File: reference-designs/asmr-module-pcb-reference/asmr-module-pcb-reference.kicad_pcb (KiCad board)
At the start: 2 copper layers, 136 x 71 mm, 1 part

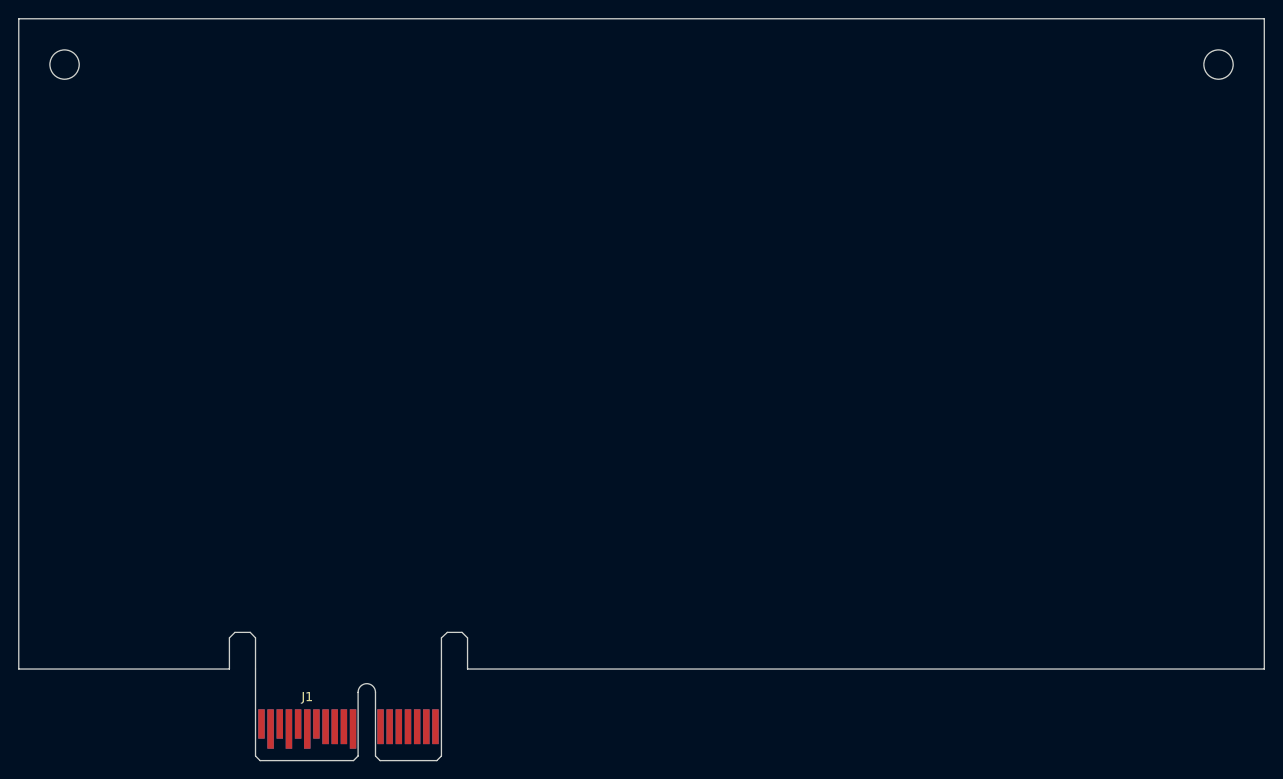
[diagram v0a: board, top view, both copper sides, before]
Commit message: Update reference design for 64-pin edge connector.
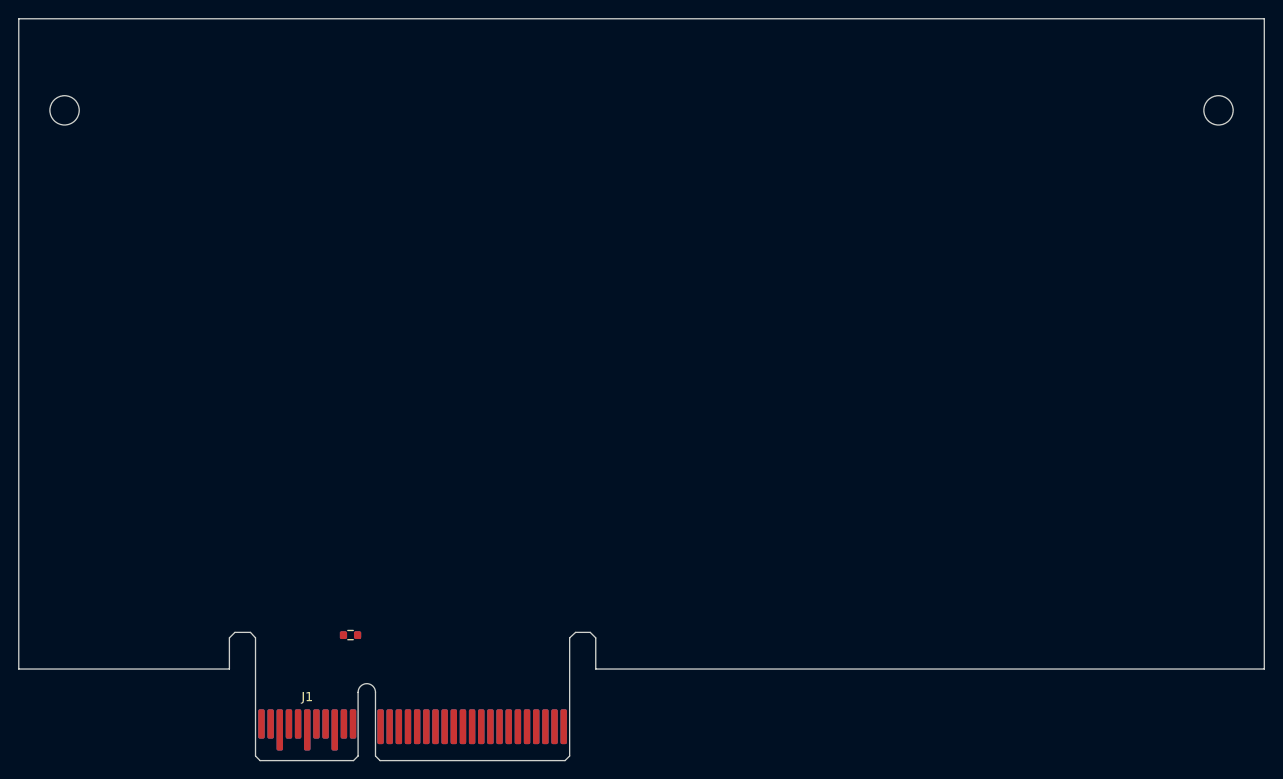
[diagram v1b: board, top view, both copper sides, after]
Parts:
- added R1: 560/1%, CM_Resistor_Capacitor:R_0603_1608Metric, F.Cu at (118.2, 111.3)
- J1: footprint CM_Connector_Edge:ASMR-Edge-36 -> CM_Connector_Edge:ASMR-Edge-64
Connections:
- J1 pad A10: unconnected-(J1-CV-PadA10) -> +5V
- J1 pad A11: GNDS -> +5V
- J1 pad A12: unconnected-(J1-Slot-PadA12) -> Net-(J1-Slot)
- J1 pad A16: unconnected-(J1-Patch8-PadA16) -> GNDS
- J1 pad A2: GND -> +24V
- J1 pad A3: +15V -> GND_CH
- J1 pad A4: GND -> +15V
- J1 pad A5: -15V -> +15V
- J1 pad A6: GND -> GND_CH
- J1 pad A7: +5V -> -15V
- J1 pad A8: unconnected-(J1-ComA-SCK-PadA8) -> -15V
- J1 pad A9: unconnected-(J1-ComB-SCK-PadA9) -> GND_CH
- J1 pad B10: unconnected-(J1-Gate-PadB10) -> +5V
- J1 pad B11: GNDS -> +5V
- J1 pad B16: unconnected-(J1-Patch7-PadB16) -> GNDS
- J1 pad B2: GND -> +24V
- J1 pad B3: +15V -> GND_CH
- J1 pad B4: GND -> +15V
- J1 pad B5: -15V -> +15V
- J1 pad B6: GND -> GND_CH
- J1 pad B7: +5V -> -15V
- J1 pad B8: unconnected-(J1-ComA-SDA-PadB8) -> -15V
- J1 pad B9: unconnected-(J1-ComB-SDA-PadB9) -> GND_CH
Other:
- outline, holes or cut-outs redrawn
- board text removed: "Card Socket"
- board text removed: "Chassis Inner Wall"
- board text removed: "Courtyard Shape: Suggested Bracket to hold PCB to Face Plate (2 places)"
- board text removed: "FACE PLATE"
- board text removed: "Maximum Allowed PCB Perimeter"
- board text removed: "PCB Backplane"
- board text removed: "Rail"
- board text removed: "Rail Clearance"
- board text removed: "Space Reserved for Chassis Features."
